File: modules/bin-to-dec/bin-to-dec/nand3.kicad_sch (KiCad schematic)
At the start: 6 parts, among them Q75 DMP3099L, Q76 2N7002, Q77 2N7002, Q78 2N7002, Q79 DMP3099L, Q80 DMP3099L

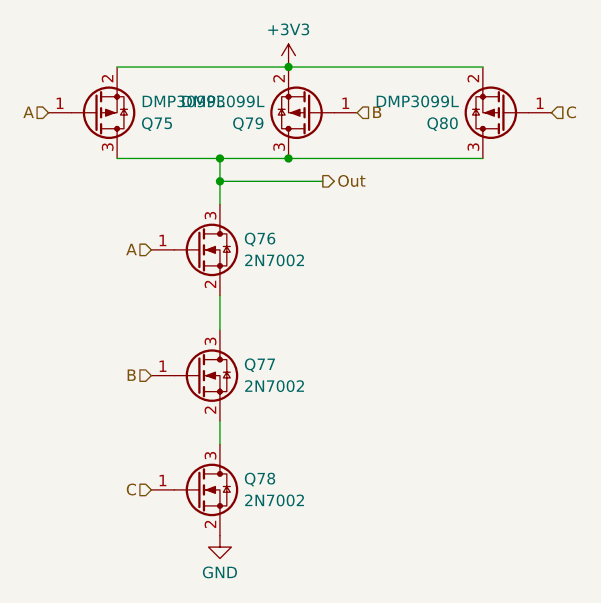
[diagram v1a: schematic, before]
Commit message: went from routed bin-to-dec to gate only
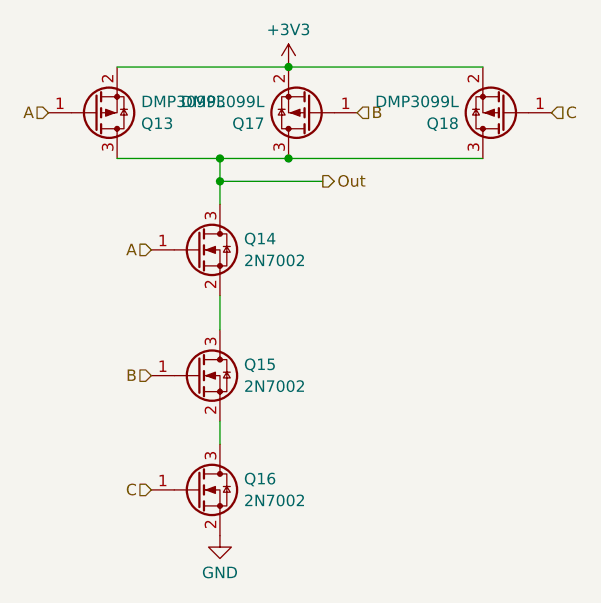
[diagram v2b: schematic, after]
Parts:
- renumbered Q75 to Q13, Q76 to Q14, Q77 to Q15, Q78 to Q16, Q79 to Q17, Q80 to Q18
